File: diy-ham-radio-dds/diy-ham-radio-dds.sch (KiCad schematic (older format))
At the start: 30 parts, among them Q1 Q_NPN_BCE, Q2 Q_NPN_BCE, Q3 Q_NPN_BCE, SW1 SW_Push, SW2 SW_Push, SW3 SW_Push, SW4 SW_Push, SW5 Rotary_Encoder_Switch, U1 L7805, U2 ATmega328-AU, Y1 Crystal_Small

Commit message: Work in progress
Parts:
- added J?: Conn_02x03_Odd_Even, symbol Connector_Generic:Conn_02x03_Odd_Even
- added J?: Screw_Terminal_01x12, symbol Connector:Screw_Terminal_01x12
- added R10, R11, R12, R13, R2, R3, R8, R9: R_Small, symbol Device:R_Small
- added TP1, TP2, TP3, TP4, TP5, TP6: TestPoint, symbol Connector:TestPoint
- renumbered C9 to C10, C10 to C9, R2 to R4, R3 to R5, R4 to R6, R5 to R7
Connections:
- net GND: now also R10.1, R13.1; no longer RV2.3, RV3.3
- net POT_1: now also R9.1; no longer RV2.2
- net POT_2: now also R12.1; no longer RV3.2
- net SCL: now also R3.1
- net SDA: now also R2.1
- net SW1: now also U2.14 (PB2); no longer U2.12 (PB0)
- net SW2: now also U2.15 (PB3); no longer U2.13 (PB1)
- net SW3: now also U2.13 (PB1); no longer U2.14 (PB2)
- net SW4: now also U2.16 (PB4); no longer U2.15 (PB3)
- net SW_ROT: now also U2.12 (PB0); no longer U2.16 (PB4)
- net VCC: now also R11.1, R2.2, R3.2, R8.1; no longer RV2.1, RV3.1
- new net: R8.2, RV2.1, TP1.1
- new net: R9.2, RV2.2, TP5.1
- new net: R10.2, RV2.3, TP2.1
- new net: R11.2, RV3.1, TP3.1
- new net: R12.2, RV3.2, TP6.1
- new net: R13.2, RV3.3, TP4.1
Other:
- note added: "ICSP"
- moved on the sheet: C10, C9, Q1, Q2, Q3, R5, R6, R7, RV2, SW5

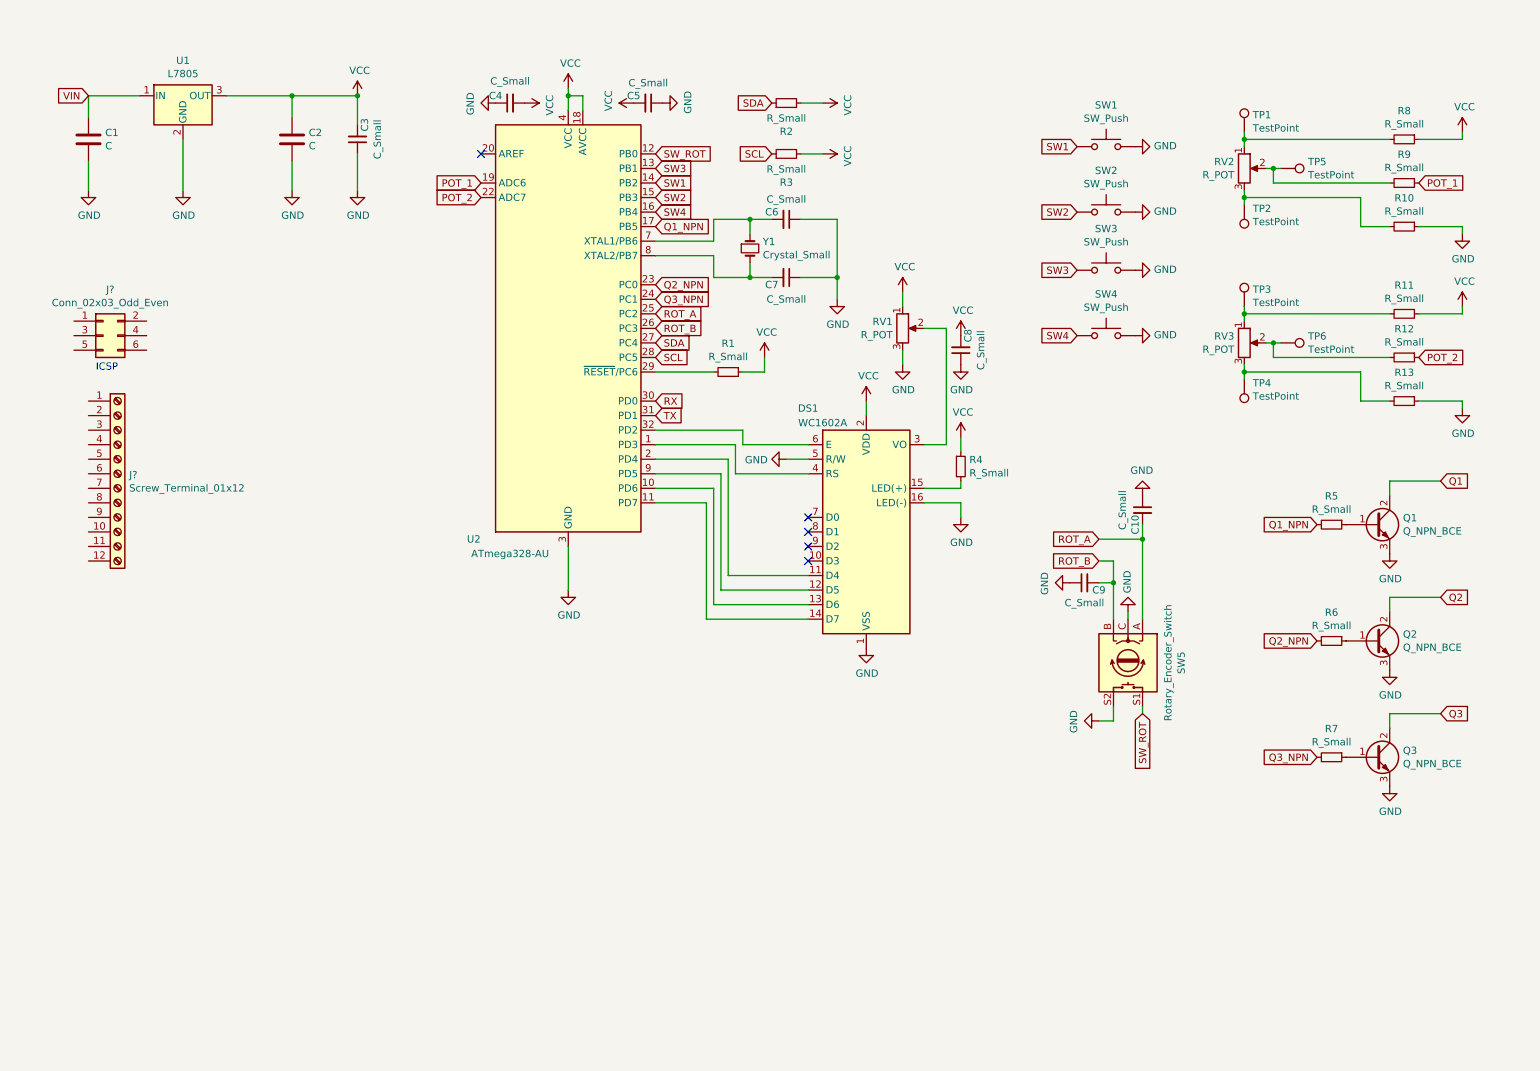
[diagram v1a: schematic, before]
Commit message: Routed display line signals
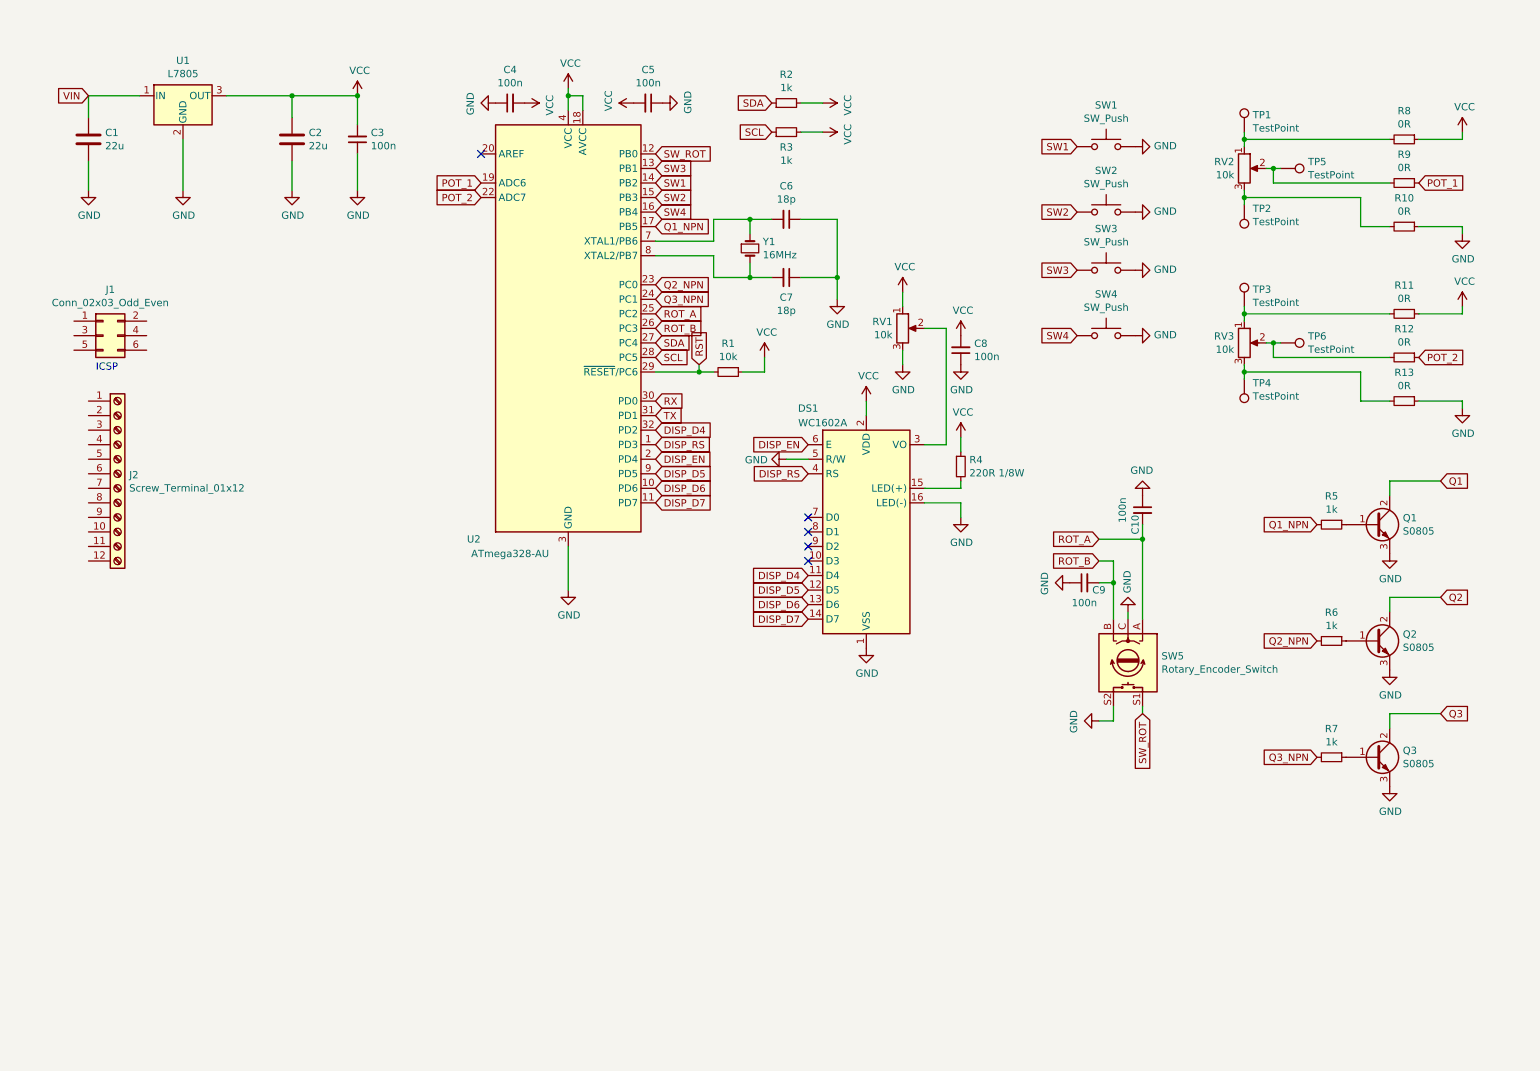
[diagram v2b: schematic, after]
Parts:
- C1, C2: value C -> 22u
- C10, C3, C4, C5, C8, C9: value C_Small -> 100n
- C6, C7: value C_Small -> 18p
- Q1, Q2, Q3: value Q_NPN_BCE -> S0805
- R1: value R_Small -> 10k
- R10, R11, R12, R13, R8, R9: value R_Small -> 0R
- R2, R3, R5, R6, R7: value R_Small -> 1k
- R4: value R_Small -> 220R 1/8W
- RV1: value R_POT -> 10k; footprint (none) -> Potentiometer_THT:Potentiometer_Alpha_RD901F-40-00D_Single_Vertical
- RV2, RV3: value R_POT -> 10k; footprint Potentiometer_THT:Potentiometer_ACP_CA9-V10_Vertical_Hole -> Potentiometer_THT:Potentiometer_Alpha_RD901F-40-00D_Single_Vertical
- Y1: value Crystal_Small -> 16MHz
- gave numbers to parts that had none: 2
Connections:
- net DISP_D4: now reaches DS1.11 (D4)
- net DISP_D4: now also U2.32 (PD2); no longer U2.2 (PD4)
- net DISP_D5: now reaches DS1.12 (D5), U2.9 (PD5)
- net DISP_D6: now reaches DS1.13 (D6), U2.10 (PD6)
- net DISP_D7: now reaches DS1.14 (D7), U2.11 (PD7)
- net DISP_RS: now reaches DS1.4 (RS), U2.1 (PD3)
- net DISP_EN: now reaches DS1.6 (E)
- net DISP_EN: now also U2.2 (PD4); no longer U2.32 (PD2)
- net RST: now reaches R1.2, U2.29 (~RESET~/PC6)
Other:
- moved on the sheet: R3

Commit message: Created minimal firmware from hardware specification
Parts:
- added U4: 74HC595, symbol 74xx:74HC595
- added U? (x5): 74LS08, symbol 74xx:74LS08
- renumbered C4 to C2, C5 to C3, C2 to C4, C3 to C5, U2 to U1, U1 to U2
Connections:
- net GND: now also U4.13 (~OE), U4.8 (GND), U?.7 (GND)
- net VCC: now also U4.10 (~SRCLR), U4.16 (VCC), U?.14 (VCC)
- net DISP_D5 renamed DISP_D5\SHIFT_DATA
- net DISP_D5\SHIFT_DATA: now also U?.2
- net DISP_D6 renamed DISP_D6\SHIFT_LATCH
- net DISP_D6\SHIFT_LATCH: now also U?.5
- net DISP_D7 renamed DISP_D7\SHIFT_CLOCK
- net DISP_D7\SHIFT_CLOCK: now also U?.10
- net Q3_NPN: no longer names the net of R7.2
- net Q3_NPN: no longer U1.24 (PC1)
- new net SHIFT_CLOCK: U4.11 (SRCLK), U?.8
- new net SHIFT_DATA: U4.14 (SER), U?.3
- new net SHIFT_ENABLE: U1.24 (PC1), U?.1, U?.12, U?.4, U?.9
- new net SHIFT_LATCH: U4.12 (RCLK), U?.6
- no-connect marks 5 -> 6
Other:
- moved on the sheet: C2, C3, C6, C7, C8, DS1, J1, J2, R1, R2, R3, R4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
